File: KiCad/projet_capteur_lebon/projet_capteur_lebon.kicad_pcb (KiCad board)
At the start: 2 copper layers, 68.6 x 53.3 mm, 9 parts, among them J1 Power, J2 Digital/PWM, J3 Analog, J4 Digital/PWM

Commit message: mep modele 3d flex s
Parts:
- added U2: ~, librairie_empreintes:SIP-2, F.Cu at (121.0, 97.0)
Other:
- board text removed: "ICSP"
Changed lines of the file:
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@@
 	(net 31 "unconnected-(U1-GND-Pad1)")
 	(net 32 "unconnected-(U1-VCC-Pad2)")
+	(net 33 "unconnected-(U2-VCC-Pad2)")
+	(net 34 "unconnected-(U2-GND-Pad1)")
 	(footprint "Connector_PinSocket_2.54mm:PinSocket_1x08_P2.54mm_Vertical"
 		(locked yes)
@@
 		(embedded_fonts no)
 	)
+	(footprint "librairie_empreintes:SIP-2"
+		(layer "F.Cu")
+		(at 121 97)
+		(property "Reference" "U2"
+			(at 0 1.75 0)
+			(layer "F.SilkS")
+			(hide yes)
+			(effects
+				(font
+					(size 1 1)
+					(thickness 0.15)
+				)
+			)
+		)
+		(property "Value" "~"
+			(at 0 -3.25 0)
+			(layer "F.Fab")
+			(hide yes)
+			(effects
+				(font
+					(size 1 1)
+					(thickness 0.15)
+				)
+			)
+		)
+		(property "Datasheet" ""
+			(at 0 -0.75 0)
+			(layer "F.Fab")
+			(hide yes)
+			(effects
+				(font
+					(size 1.27 1.27)
+					(thickness 0.15)
+				)
+			)
+		)
+		(property "Description" ""
+			(at 0 -0.75 0)
+			(layer "F.Fab")
+			(hide yes)
+			(effects
+				(font
+					(size 1.27 1.27)
+					(thickness 0.15)
+				)
+			)
+		)
+		(sheetname "/")
+		(sheetfile "projet_capteur_lebon.kicad_sch")
+		(attr through_hole)
+		(fp_line
+			(start -2.95 -2.25)
+			(end 2.95 -2.25)
+			(stroke
+				(width 0.12)
+				(type default)
+			)
+			(layer "F.SilkS")
+		)
+		(fp_line
+			(start -2.95 0.75)
+			(end -2.95 -2.25)
+			(stroke
+				(width 0.12)
+				(type default)
+			)
+			(layer "F.SilkS")
+		)
+		(fp_line
+			(start 0 -2.25)
+			(end 0 0.75)
+			(stroke
+				(width 0.12)
+				(type default)
+			)
+			(layer "F.SilkS")
+		)
+		(fp_line
+			(start 2.95 -2.25)
+			(end 2.95 0.75)
+			(stroke
+				(width 0.12)
+				(type default)
+			)
+			(layer "F.SilkS")
+		)
+		(fp_line
+			(start 2.95 0.75)
+			(end -2.95 0.75)
+			(stroke
+				(width 0.12)
+				(type default)
+			)
+			(layer "F.SilkS")
+		)
+		(fp_rect
+			(start -4.5 -2.5)
+			(end 4.5 2.5)
+			(stroke
+				(width 0.1)
+				(type default)
+			)
+			(fill no)
+			(layer "F.SilkS")
+		)
+		(fp_line
+			(start -2.7 -2)
+			(end 2.7 -2)
+			(stroke
+				(width 0.05)
+				(type default)
+			)
+			(layer "F.CrtYd")
+		)
+		(fp_line
+			(start -2.7 0.5)
+			(end -2.7 -2)
+			(stroke
+				(width 0.05)
+				(type default)
+			)
+			(layer "F.CrtYd")
+		)
+		(fp_line
+			(start 2.7 -2)
+			(end 2.7 0.5)
+			(stroke
+				(width 0.05)
+				(type default)
+			)
+			(layer "F.CrtYd")
+		)
+		(fp_line
+			(start 2.7 0.5)
+			(end -2.7 0.5)
+			(stroke
+				(width 0.05)
+				(type default)
+			)
+			(layer "F.CrtYd")
+		)
+		(fp_text user "FLEXS"
+			(at -2.5 2.5 0)
+			(unlocked yes)
+			(layer "F.SilkS")
+			(effects
+				(font
+					(size 1 1)
+					(thickness 0.1)
+				)
+				(justify left bottom)
+			)
+		)
+		(pad "1" thru_hole circle
+			(at -1.45 -0.75)
+			(size 2 2)
+			(drill 0.8)
+			(layers "*.Cu" "*.Mask")
+			(remove_unused_layers no)
+			(net 34 "unconnected-(U2-GND-Pad1)")
+			(pinfunction "GND")
+			(pintype "input")
+		)
+		(pad "2" thru_hole circle
+			(at 1.45 -0.75)
+			(size 2 2)
+			(drill 0.8)
+			(layers "*.Cu" "*.Mask")
+			(remove_unused_layers no)
+			(net 33 "unconnected-(U2-VCC-Pad2)")
+			(pinfunction "VCC")
+			(pintype "input")
+		)
+		(embedded_fonts no)
+		(model "C:/Users/clara/OneDrive/Documents/INSA/4A/Capteurs/2024-2025-4GP-Anatolie-Clara/KiCad/Modele 3D/FS-L-0095-103-ST - Assembly.stp"
+			(offset
+				(xyz 0 1.5 0)
+			)
+			(scale
+				(xyz 1 1 1)
+			)
+			(rotate
+				(xyz -0 -0 -0)
+			)
+		)
+	)
 	(footprint "Arduino_MountingHole:MountingHole_3.2mm"
 		(locked yes)
@@
 		(layer "Dwgs.User")
 	)
-	(gr_rect
-		(start 162.357 68.25)
-		(end 167.437 75.87)
-		(stroke
-			(width 0.15)
-			(type solid)
-		)
-		(fill no)
-		(layer "Dwgs.User")
-	)
 	(gr_line
 		(start 98.095 87.935)
@@
 		(layer "Edge.Cuts")
 	)
-	(gr_text "ICSP"
-		(at 164.897 72.06 90)
-		(layer "Dwgs.User")
-		(effects
-			(font
-				(size 1 1)
-				(thickness 0.15)
-			)
-		)
-	)
 	(embedded_fonts no)

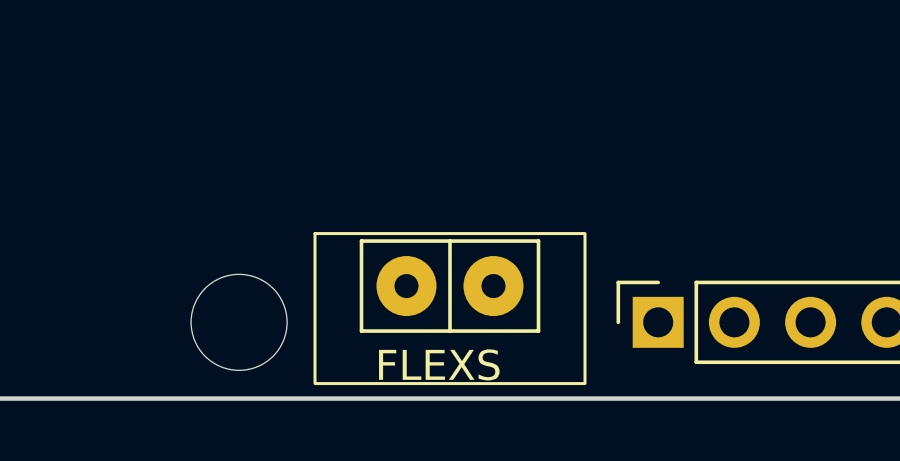
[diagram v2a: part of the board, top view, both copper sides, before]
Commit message: modif flex sensor
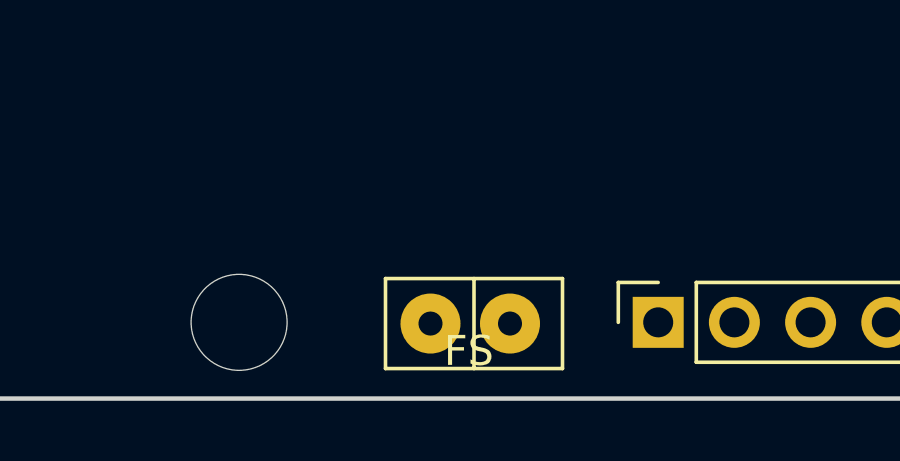
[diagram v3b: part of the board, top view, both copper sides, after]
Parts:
- moved U2 1.48 mm to (121.8, 98.2)
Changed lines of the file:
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@@
+		)
+	)
+	(footprint "librairie_empreintes:SIP-2"
+		(layer "F.Cu")
+		(at 121.8 98.25)
+		(property "Reference" "U2"
+			(at 0 1.75 0)
+			(layer "F.SilkS")
+			(hide yes)
+			(effects
+				(font
+					(size 1 1)
+					(thickness 0.15)
+				)
+			)
+		)
+		(property "Value" "~"
+			(at 0 -3.25 0)
+			(layer "F.Fab")
+			(hide yes)
+			(effects
+				(font
+					(size 1 1)
+					(thickness 0.15)
+				)
+			)
+		)
+		(property "Datasheet" ""
+			(at 0 -0.75 0)
+			(layer "F.Fab")
+			(hide yes)
+			(effects
+				(font
+					(size 1.27 1.27)
+					(thickness 0.15)
+				)
+			)
+		)
+		(property "Description" ""
+			(at 0 -0.75 0)
+			(layer "F.Fab")
+			(hide yes)
+			(effects
+				(font
+					(size 1.27 1.27)
+					(thickness 0.15)
+				)
+			)
+		)
+		(sheetname "/")
+		(sheetfile "projet_capteur_lebon.kicad_sch")
+		(attr through_hole)
+		(fp_line
+			(start -2.95 -2.25)
+			(end 2.95 -2.25)
+			(stroke
+				(width 0.12)
+				(type default)
+			)
+			(layer "F.SilkS")
+		)
+		(fp_line
+			(start -2.95 0.75)
+			(end -2.95 -2.25)
+			(stroke
+				(width 0.12)
+				(type default)
+			)
+			(layer "F.SilkS")
+		)
+		(fp_line
+			(start 0 -2.25)
+			(end 0 0.75)
+			(stroke
+				(width 0.12)
+				(type default)
+			)
+			(layer "F.SilkS")
+		)
+		(fp_line
+			(start 2.95 -2.25)
+			(end 2.95 0.75)
+			(stroke
+				(width 0.12)
+				(type default)
+			)
+			(layer "F.SilkS")
+		)
+		(fp_line
+			(start 2.95 0.75)
+			(end -2.95 0.75)
+			(stroke
+				(width 0.12)
+				(type default)
+			)
+			(layer "F.SilkS")
+		)
+		(fp_line
+			(start -2.7 -2)
+			(end 2.7 -2)
+			(stroke
+				(width 0.05)
+				(type default)
+			)
+			(layer "F.CrtYd")
+		)
+		(fp_line
+			(start -2.7 0.5)
+			(end -2.7 -2)
+			(stroke
+				(width 0.05)
+				(type default)
+			)
+			(layer "F.CrtYd")
+		)
+		(fp_line
+			(start 2.7 -2)
+			(end 2.7 0.5)
+			(stroke
+				(width 0.05)
+				(type default)
+			)
+			(layer "F.CrtYd")
+		)
+		(fp_line
+			(start 2.7 0.5)
+			(end -2.7 0.5)
+			(stroke
+				(width 0.05)
+				(type default)
+			)
+			(layer "F.CrtYd")
+		)
+		(fp_text user "FS"
+			(at -1 0.75 0)
+			(unlocked yes)
+			(layer "F.SilkS")
+			(effects
+				(font
+					(size 1 1)
+					(thickness 0.1)
+				)
+				(justify left bottom)
+			)
+		)
+		(pad "1" thru_hole circle
+			(at -1.45 -0.75)
+			(size 2 2)
+			(drill 0.8)
+			(layers "*.Cu" "*.Mask")
+			(remove_unused_layers no)
+			(net 34 "unconnected-(U2-GND-Pad1)")
+			(pinfunction "GND")
+			(pintype "input")
+		)
+		(pad "2" thru_hole circle
+			(at 1.2 -0.75)
+			(size 2 2)
+			(drill 0.8)
+			(layers "*.Cu" "*.Mask")
+			(remove_unused_layers no)
+			(net 33 "unconnected-(U2-VCC-Pad2)")
+			(pinfunction "VCC")
+			(pintype "input")
+		)
+		(embedded_fonts no)
+		(model "C:/Users/clara/OneDrive/Documents/INSA/4A/Capteurs/2024-2025-4GP-Anatolie-Clara/KiCad/Modele 3D/FS-L-0095-103-ST - Assembly.stp"
+			(offset
+				(xyz 0 1 0.5)
+			)
+			(scale
+				(xyz 1 1 1)
+			)
+			(rotate
+				(xyz -90 -0 -0)
+			)
 		)
 	)
@@
 		(embedded_fonts no)
 	)
-	(footprint "librairie_empreintes:SIP-2"
-		(layer "F.Cu")
-		(at 121 97)
-		(property "Reference" "U2"
-			(at 0 1.75 0)
-			(layer "F.SilkS")
-			(hide yes)
-			(effects
-				(font
-					(size 1 1)
-					(thickness 0.15)
-				)
-			)
-		)
-		(property "Value" "~"
-			(at 0 -3.25 0)
-			(layer "F.Fab")
-			(hide yes)
-			(effects
-				(font
-					(size 1 1)
-					(thickness 0.15)
-				)
-			)
-		)
-		(property "Datasheet" ""
-			(at 0 -0.75 0)
-			(layer "F.Fab")
-			(hide yes)
-			(effects
-				(font
-					(size 1.27 1.27)
-					(thickness 0.15)
-				)
-			)
-		)
-		(property "Description" ""
-			(at 0 -0.75 0)
-			(layer "F.Fab")
-			(hide yes)
-			(effects
-				(font
-					(size 1.27 1.27)
-					(thickness 0.15)
-				)
-			)
-		)
-		(sheetname "/")
-		(sheetfile "projet_capteur_lebon.kicad_sch")
-		(attr through_hole)
-		(fp_line
-			(start -2.95 -2.25)
-			(end 2.95 -2.25)
-			(stroke
-				(width 0.12)
-				(type default)
-			)
-			(layer "F.SilkS")
-		)
-		(fp_line
-			(start -2.95 0.75)
-			(end -2.95 -2.25)
-			(stroke
-				(width 0.12)
-				(type default)
-			)
-			(layer "F.SilkS")
-		)
-		(fp_line
-			(start 0 -2.25)
-			(end 0 0.75)
-			(stroke
-				(width 0.12)
-				(type default)
-			)
-			(layer "F.SilkS")
-		)
-		(fp_line
-			(start 2.95 -2.25)
-			(end 2.95 0.75)
-			(stroke
-				(width 0.12)
-				(type default)
-			)
-			(layer "F.SilkS")
-		)
-		(fp_line
-			(start 2.95 0.75)
-			(end -2.95 0.75)
-			(stroke
-				(width 0.12)
-				(type default)
-			)
-			(layer "F.SilkS")
-		)
-		(fp_rect
-			(start -4.5 -2.5)
-			(end 4.5 2.5)
-			(stroke
-				(width 0.1)
-				(type default)
-			)
-			(fill no)
-			(layer "F.SilkS")
-		)
-		(fp_line
-			(start -2.7 -2)
-			(end 2.7 -2)
-			(stroke
-				(width 0.05)
-				(type default)
-			)
-			(layer "F.CrtYd")
-		)
-		(fp_line
-			(start -2.7 0.5)
-			(end -2.7 -2)
-			(stroke
-				(width 0.05)
-				(type default)
-			)
-			(layer "F.CrtYd")
-		)
-		(fp_line
-			(start 2.7 -2)
-			(end 2.7 0.5)
-			(stroke
-				(width 0.05)
-				(type default)
-			)
-			(layer "F.CrtYd")
-		)
-		(fp_line
-			(start 2.7 0.5)
-			(end -2.7 0.5)
-			(stroke
-				(width 0.05)
-				(type default)
-			)
-			(layer "F.CrtYd")
-		)
-		(fp_text user "FLEXS"
-			(at -2.5 2.5 0)
-			(unlocked yes)
-			(layer "F.SilkS")
-			(effects
-				(font
-					(size 1 1)
-					(thickness 0.1)
-				)
-				(justify left bottom)
-			)
-		)
-		(pad "1" thru_hole circle
-			(at -1.45 -0.75)
-			(size 2 2)
-			(drill 0.8)
-			(layers "*.Cu" "*.Mask")
-			(remove_unused_layers no)
-			(net 34 "unconnected-(U2-GND-Pad1)")
-			(pinfunction "GND")
-			(pintype "input")
-		)
-		(pad "2" thru_hole circle
-			(at 1.45 -0.75)
-			(size 2 2)
-			(drill 0.8)
-			(layers "*.Cu" "*.Mask")
-			(remove_unused_layers no)
-			(net 33 "unconnected-(U2-VCC-Pad2)")
-			(pinfunction "VCC")
-			(pintype "input")
-		)
-		(embedded_fonts no)
-		(model "C:/Users/clara/OneDrive/Documents/INSA/4A/Capteurs/2024-2025-4GP-Anatolie-Clara/KiCad/Modele 3D/FS-L-0095-103-ST - Assembly.stp"
-			(offset
-				(xyz 0 1.5 0)
-			)
-			(scale
-				(xyz 1 1 1)
-			)
-			(rotate
-				(xyz -0 -0 -0)
-			)
-		)
-	)
 	(footprint "Arduino_MountingHole:MountingHole_3.2mm"

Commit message: creation ampli
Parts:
- added U3: ~, librairie_empreintes:DIP-8_296, F.Cu at (118.2, 79.7)
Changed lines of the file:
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@@
 	(net 33 "unconnected-(U2-VCC-Pad2)")
 	(net 34 "unconnected-(U2-GND-Pad1)")
+	(net 35 "unconnected-(U3-VCC--Pad4)")
+	(net 36 "unconnected-(U3-OUT-Pad6)")
+	(net 37 "unconnected-(U3-IN+-Pad3)")
+	(net 38 "unconnected-(U3-VCC+-Pad7)")
+	(net 39 "unconnected-(U3-NC-Pad8)")
+	(net 40 "unconnected-(U3-CLK-Pad5)")
+	(net 41 "unconnected-(U3-IN--Pad2)")
+	(net 42 "unconnected-(U3-NC-Pad1)")
 	(footprint "Connector_PinSocket_2.54mm:PinSocket_1x08_P2.54mm_Vertical"
 		(locked yes)
@@
 		)
 		(embedded_fonts no)
+	)
+	(footprint "librairie_empreintes:DIP-8_296"
+		(layer "F.Cu")
+		(at 118.19 79.74)
+		(property "Reference" "U3"
+			(at -6.31 0 90)
+			(layer "F.SilkS")
+			(hide yes)
+			(effects
+				(font
+					(size 1 1)
+					(thickness 0.15)
+				)
+			)
+		)
+		(property "Value" "~"
+			(at 0 0 0)
+			(layer "F.Fab")
+			(hide yes)
+			(effects
+				(font
+					(size 1 1)
+					(thickness 0.15)
+				)
+			)
+		)
+		(property "Datasheet" ""
+			(at 0 0 0)
+			(layer "F.Fab")
+			(hide yes)
+			(effects
+				(font
+					(size 1.27 1.27)
+					(thickness 0.15)
+				)
+			)
+		)
+		(property "Description" ""
+			(at 0 0 0)
+			(layer "F.Fab")
+			(hide yes)
+			(effects
+				(font
+					(size 1.27 1.27)
+					(thickness 0.15)
+				)
+			)
+		)
+		(sheetname "/")
+		(sheetfile "projet_capteur_lebon.kicad_sch")
+		(attr through_hole)
+		(fp_rect
+			(start -5 -5)
+			(end 5 5)
+			(stroke
+				(width 0.1)
+				(type default)
+			)
+			(fill no)
+			(layer "F.SilkS")
+		)
+		(fp_circle
+			(center -5 0)
+			(end -3.5 0)
+			(stroke
+				(width 0.1)
+				(type default)
+			)
+			(fill no)
+			(layer "F.SilkS")
+		)
+		(fp_text user "AO"
+			(at -1 2.5 0)
+			(unlocked yes)
+			(layer "F.SilkS")
+			(effects
+				(font
+					(size 1 1)
+					(thickness 0.1)
+				)
+				(justify left bottom)
+			)
+		)
+		(pad "1" thru_hole rect
+			(at -3.81 3.76)
+			(size 2 2)
+			(drill 0.8)
+			(layers "*.Cu" "*.Mask")
+			(remove_unused_layers no)
+			(net 42 "unconnected-(U3-NC-Pad1)")
+			(pinfunction "NC")
+			(pintype "input")
+		)
+		(pad "2" thru_hole circle
+			(at -1.27 3.76)
+			(size 2 2)
+			(drill 0.8)
+			(layers "*.Cu" "*.Mask")
+			(remove_unused_layers no)
+			(net 41 "unconnected-(U3-IN--Pad2)")
+			(pinfunction "IN-")
+			(pintype "input")
+		)
+		(pad "3" thru_hole circle
+			(at 1.27 3.76)
+			(size 2 2)
+			(drill 0.8)
+			(layers "*.Cu" "*.Mask")
+			(remove_unused_layers no)
+			(net 37 "unconnected-(U3-IN+-Pad3)")
+			(pinfunction "IN+")
+			(pintype "input")
+		)
+		(pad "4" thru_hole circle
+			(at 3.81 3.76)
+			(size 2 2)
+			(drill 0.8)
+			(layers "*.Cu" "*.Mask")
+			(remove_unused_layers no)
+			(net 35 "unconnected-(U3-VCC--Pad4)")
+			(pinfunction "VCC-")
+			(pintype "input")
+		)
+		(pad "5" thru_hole circle
+			(at 3.81 -3.76)
+			(size 2 2)
+			(drill 0.8)
+			(layers "*.Cu" "*.Mask")
+			(remove_unused_layers no)
+			(net 40 "unconnected-(U3-CLK-Pad5)")
+			(pinfunction "CLK")
+			(pintype "input")
+		)
+		(pad "6" thru_hole circle
+			(at 1.27 -3.76)
+			(size 2 2)
+			(drill 0.8)
+			(layers "*.Cu" "*.Mask")
+			(remove_unused_layers no)
+			(net 36 "unconnected-(U3-OUT-Pad6)")
+			(pinfunction "OUT")
+			(pintype "output")
+		)
+		(pad "7" thru_hole circle
+			(at -1.27 -3.76)
+			(size 2 2)
+			(drill 0.8)
+			(layers "*.Cu" "*.Mask")
+			(remove_unused_layers no)
+			(net 38 "unconnected-(U3-VCC+-Pad7)")
+			(pinfunction "VCC+")
+			(pintype "input")
+		)
+		(pad "8" thru_hole circle
+			(at -3.81 -3.76)
+			(size 2 2)
+			(drill 0.8)
+			(layers "*.Cu" "*.Mask")
+			(remove_unused_layers no)
+			(net 39 "unconnected-(U3-NC-Pad8)")
+			(pinfunction "NC")
+			(pintype "input")
+		)
+		(embedded_fonts no)

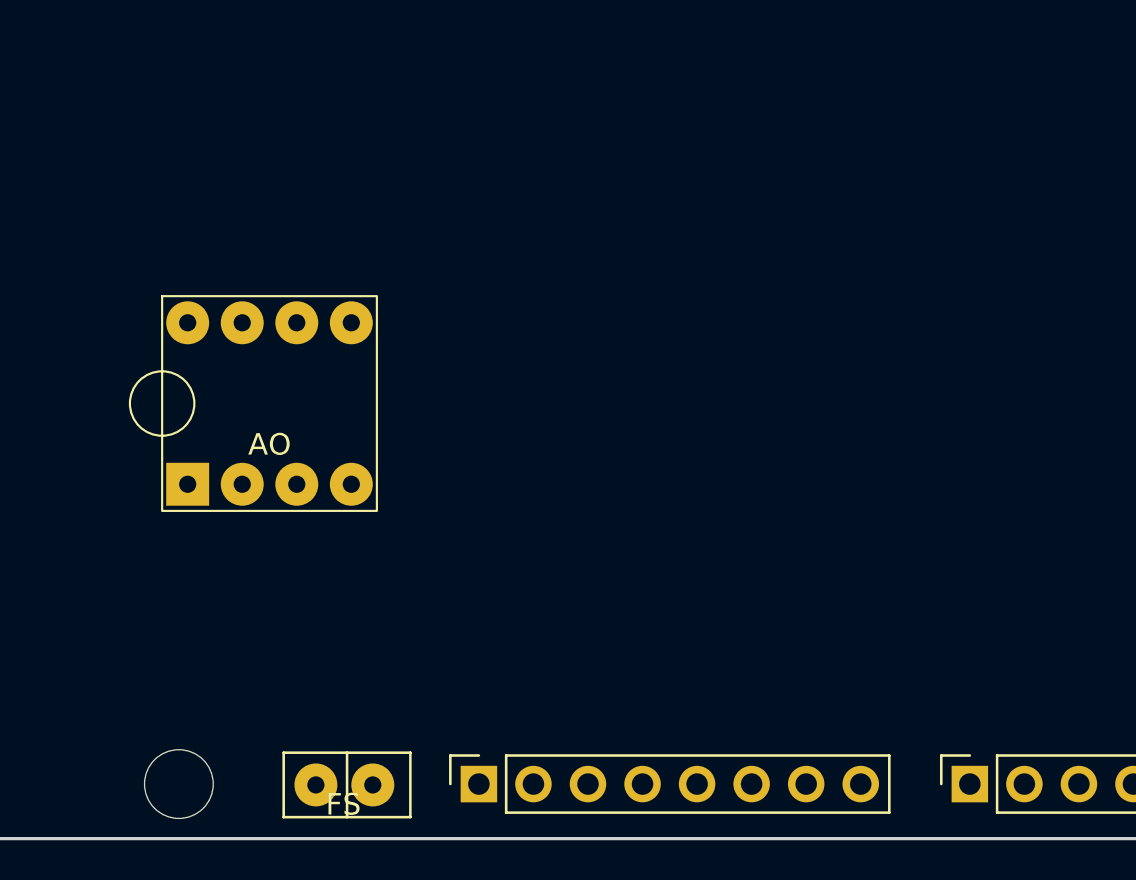
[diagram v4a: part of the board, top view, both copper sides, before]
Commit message: travail sur l'ampli transimpedance
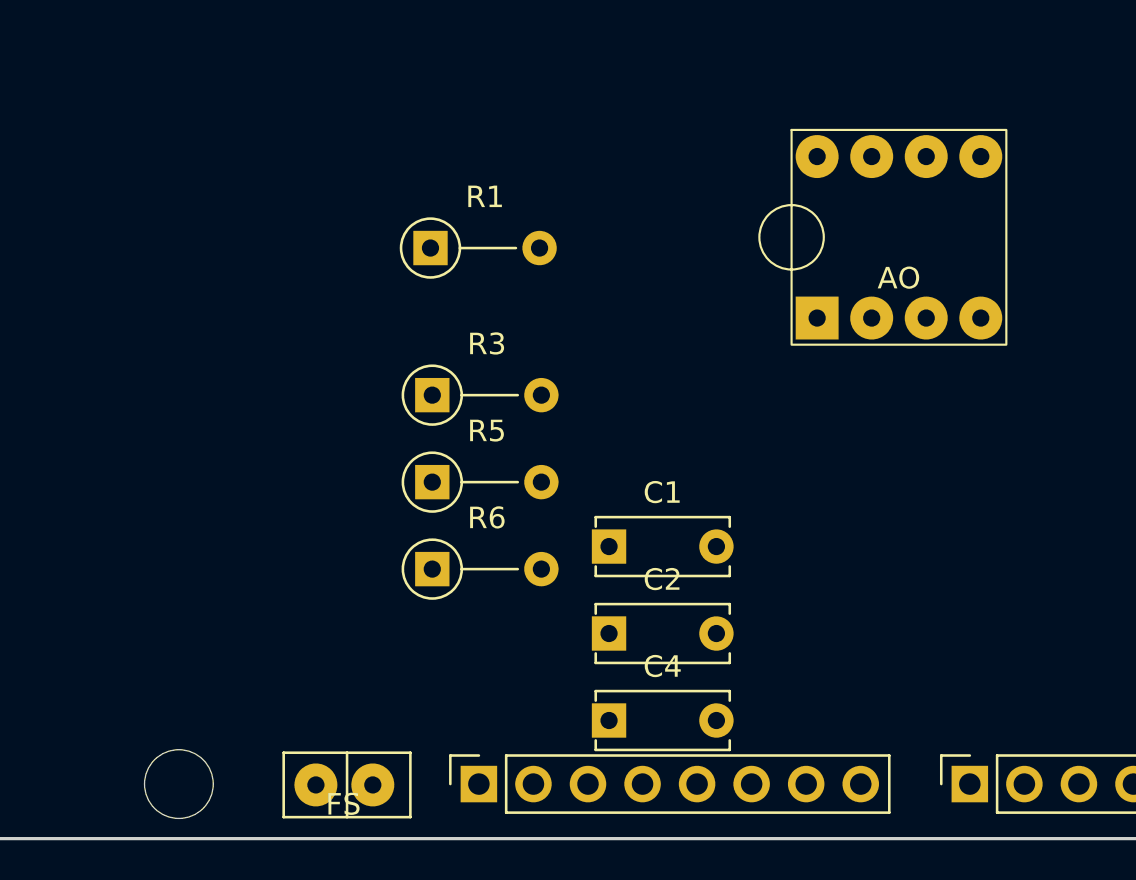
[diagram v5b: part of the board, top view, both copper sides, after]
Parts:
- removed U3: ~, librairie_empreintes:DIP-8_296
- added C1: 100n, librairie_empreintes:C_Disc_D6.0mm_W2.5mm_P5.00mm, F.Cu at (134.0, 86.4)
- added C2: 100n, librairie_empreintes:C_Disc_D6.0mm_W2.5mm_P5.00mm, F.Cu at (134.0, 90.5)
- added C4: 1u, librairie_empreintes:C_Disc_D6.0mm_W2.5mm_P5.00mm, F.Cu at (134.0, 94.5)
- added R1: 100k, librairie_empreintes:R_Axial_DIN0207_L6.3mm_D2.5mm_P5.08mm_Vertical, F.Cu at (125.7, 72.5)
- added R3: 100k, librairie_empreintes:R_Axial_DIN0207_L6.3mm_D2.5mm_P5.08mm_Vertical, F.Cu at (125.8, 79.3)
- added R5: 10k, librairie_empreintes:R_Axial_DIN0207_L6.3mm_D2.5mm_P5.08mm_Vertical, F.Cu at (125.8, 83.4)
- added R6: 1k, librairie_empreintes:R_Axial_DIN0207_L6.3mm_D2.5mm_P5.08mm_Vertical, F.Cu at (125.8, 87.5)
- added U4: ~, librairie_empreintes:DIP-8_296, F.Cu at (147.5, 72.0)
